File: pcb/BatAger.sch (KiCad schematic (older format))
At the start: 23 parts

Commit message: Added multiple schematic pages.
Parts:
- removed D? (x2): LED, symbol LED
- removed IC?: ATMEGA328-P, DIL28, symbol ATMEGA328-P
- removed OP?: LT1097, symbol LT1097
- removed Q? (x2): BC849, SOT-23, symbol BC849
- removed Q?: CSD18536KCS, TO-220, symbol BTS141
- removed Q?: IRF9530, TO-220, symbol IRF9530
- removed R? (x13): R, symbol R
- removed U?: LM358DUAL, symbol LM358DUAL
- added IC?: ATMEGA2560-A, TQFP100, symbol ATMEGA2560-A
- added U?: LM7805, symbol LM7805
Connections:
- net labels removed: +15V, -15V, GND, VCC
- wire segments 27 -> 0
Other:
- moved on the sheet: U?

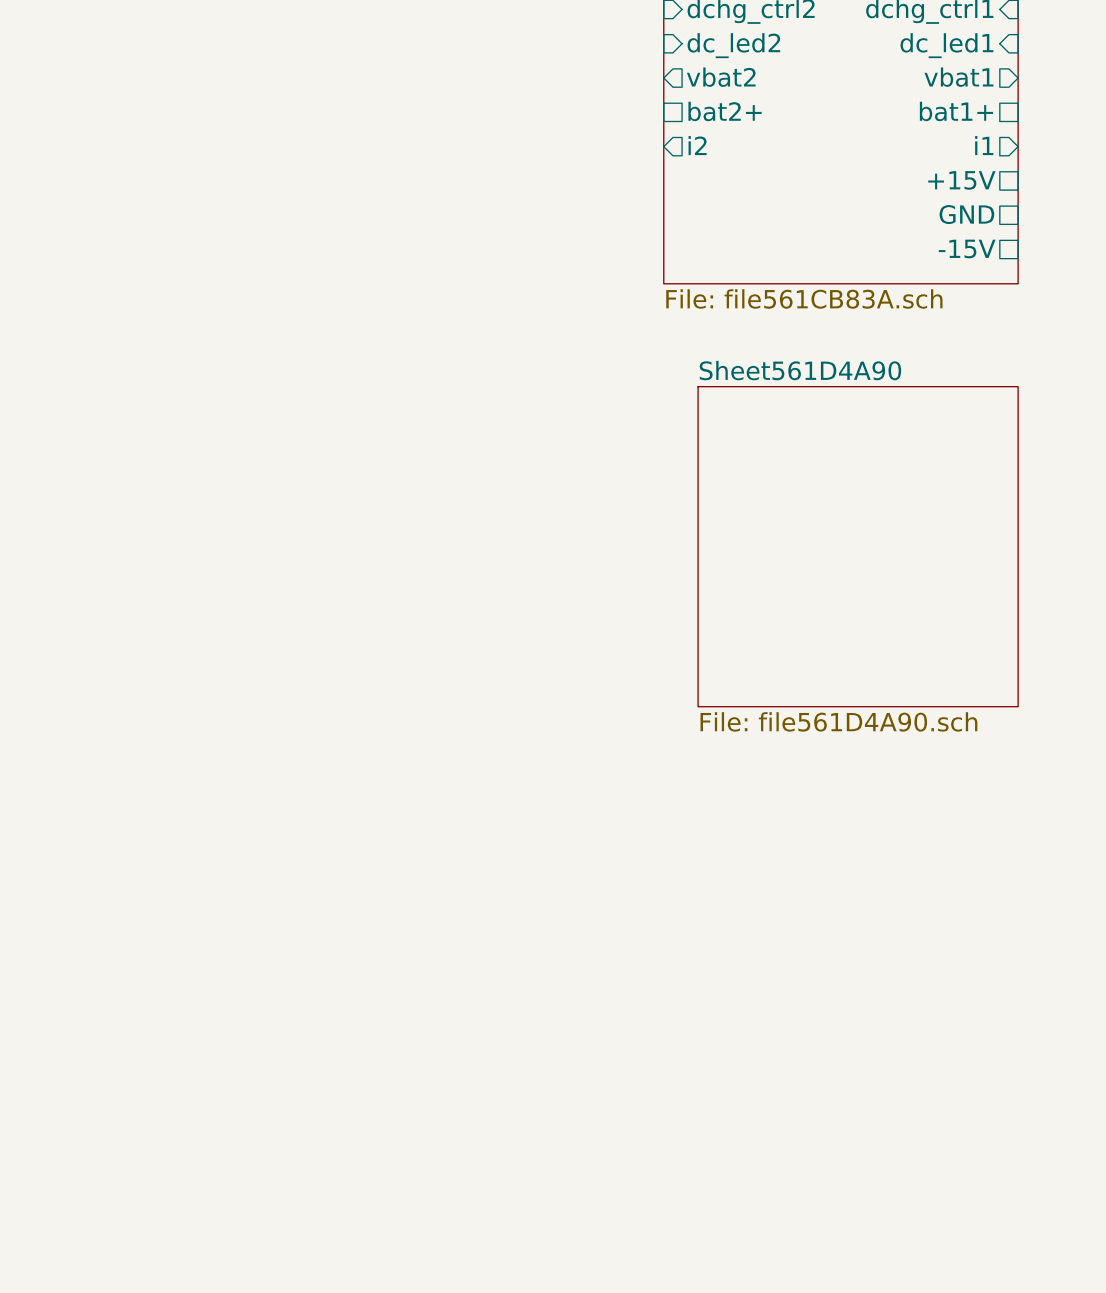
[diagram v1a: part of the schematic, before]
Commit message: updated schematics
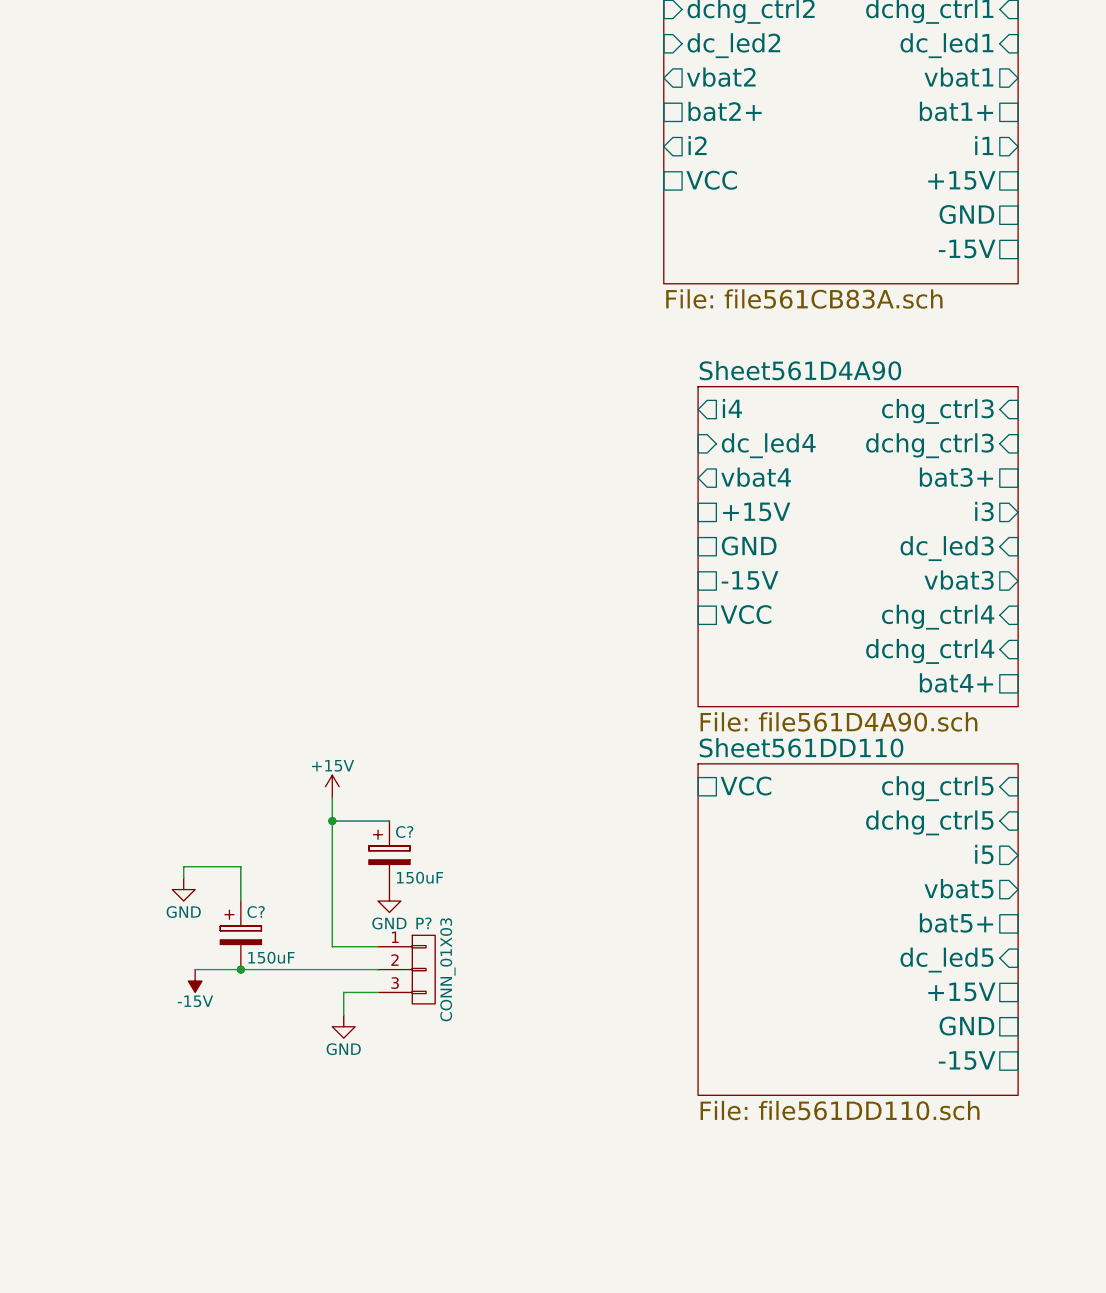
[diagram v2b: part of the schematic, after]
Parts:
- added C? (x2): 150uF, symbol CP
- added P?: CONN_01X03, symbol CONN_01X03
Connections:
- new net +15V: C?.1, P?.1 (P1)
- new net -15V: C?.2, P?.2 (P2)
- new net GND: C?.1, C?.2, P?.3 (P3)
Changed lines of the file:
@@
 $Descr A4 11693 8268
 encoding utf-8
-Sheet 1 3
+Sheet 1 4
 Title ""
 Date "12 oct 2015"
@@
 F15 "bat2+" U L 9050 1750 80
 F16 "i2" O L 9050 1900 80
+F17 "VCC" U L 9050 2050 80
 $EndSheet
 $Sheet
@@
 F0 "Sheet561D4A90" 80
 F1 "file561D4A90.sch" 80
+F2 "chg_ctrl3" I R 10600 3050 80
+F3 "dchg_ctrl3" I R 10600 3200 80
+F4 "bat3+" U R 10600 3350 80
+F5 "i3" O R 10600 3500 80
+F6 "dc_led3" I R 10600 3650 80
+F7 "vbat3" O R 10600 3800 80
+F8 "chg_ctrl4" I R 10600 3950 80
+F9 "dchg_ctrl4" I R 10600 4100 80
+F10 "bat4+" U R 10600 4250 80
+F11 "i4" O L 9200 3050 80
+F12 "dc_led4" I L 9200 3200 80
+F13 "vbat4" O L 9200 3350 80
+F14 "+15V" U L 9200 3500 80
+F15 "GND" U L 9200 3650 80
+F16 "-15V" U L 9200 3800 80
+F17 "VCC" U L 9200 3950 80
 $EndSheet
 $Comp
@@
 	1    0    0    -1
 $EndComp
+$Sheet
+S 9200 4600 1400 1450
+U 561DD111
+F0 "Sheet561DD110" 80
+F1 "file561DD110.sch" 80
+F2 "chg_ctrl5" I R 10600 4700 80
+F3 "dchg_ctrl5" I R 10600 4850 80
+F4 "i5" O R 10600 5000 80
+F5 "vbat5" O R 10600 5150 80
+F6 "bat5+" U R 10600 5300 80
+F7 "dc_led5" I R 10600 5450 80
+F8 "+15V" U R 10600 5600 80
+F9 "GND" U R 10600 5750 80
+F10 "-15V" U R 10600 5900 80
+F11 "VCC" U L 9200 4700 80
+$EndSheet
+$Comp
+L CONN_01X03 P?
+U 1 1 561DFDB9
+P 8000 5500
+F 0 "P?" H 8000 5700 50  0000 C CNN
+F 1 "CONN_01X03" V 8100 5500 50  0000 C CNN
+F 2 "" H 8000 5500 60  0000 C CNN
+F 3 "" H 8000 5500 60  0000 C CNN
+	1    8000 5500
+	1    0    0    -1
+$EndComp
+$Comp
+L +15V #PWR?
+U 1 1 561DFF64
+P 7600 4750
+F 0 "#PWR?" H 7600 4600 50  0001 C CNN
+F 1 "+15V" H 7600 4890 50  0000 C CNN
+F 2 "" H 7600 4750 60  0000 C CNN
+F 3 "" H 7600 4750 60  0000 C CNN
+	1    7600 4750
+	1    0    0    -1
+$EndComp
+$Comp
+L -15V #PWR?
+U 1 1 561E0397
+P 7000 5500
+F 0 "#PWR?" H 7000 5350 50  0001 C CNN
+F 1 "-15V" H 7000 5640 50  0000 C CNN
+F 2 "" H 7000 5500 60  0000 C CNN
+F 3 "" H 7000 5500 60  0000 C CNN
+	1    7000 5500
+	-1   0    0    1
+$EndComp
+$Comp
+L GND #PWR?
+U 1 1 561E075B
+P 7650 5700
+F 0 "#PWR?" H 7650 5450 50  0001 C CNN
+F 1 "GND" H 7650 5550 50  0000 C CNN
+F 2 "" H 7650 5700 60  0000 C CNN
+F 3 "" H 7650 5700 60  0000 C CNN
+	1    7650 5700
+	1    0    0    -1
+$EndComp
+Wire Wire Line
+	7800 5400 7600 5400
+Wire Wire Line
+	7600 5400 7600 4750
+Wire Wire Line
+	7000 5500 7800 5500
+Wire Wire Line
+	7800 5600 7650 5600
+Wire Wire Line
+	7650 5600 7650 5700
+$Comp
+L CP C?
+U 1 1 561E6331
+P 7200 5350
+F 0 "C?" H 7225 5450 50  0000 L CNN
+F 1 "150uF" H 7225 5250 50  0000 L CNN
+F 2 "" H 7238 5200 30  0000 C CNN
+F 3 "" H 7200 5350 60  0000 C CNN
+	1    7200 5350
+	1    0    0    -1
+$EndComp
+Connection ~ 7200 5500
+$Comp
+L GND #PWR?
+U 1 1 561E646E
+P 6950 5100
+F 0 "#PWR?" H 6950 4850 50  0001 C CNN
+F 1 "GND" H 6950 4950 50  0000 C CNN
+F 2 "" H 6950 5100 60  0000 C CNN
+F 3 "" H 6950 5100 60  0000 C CNN
+	1    6950 5100
+	1    0    0    -1
+$EndComp
+Wire Wire Line
+	7200 5200 7200 5050
+Wire Wire Line
+	7200 5050 6950 5050
+Wire Wire Line
+	6950 5050 6950 5100
+$Comp
+L CP C?
+U 1 1 561E67B1
+P 7850 5000
+F 0 "C?" H 7875 5100 50  0000 L CNN
+F 1 "150uF" H 7875 4900 50  0000 L CNN
+F 2 "" H 7888 4850 30  0000 C CNN
+F 3 "" H 7850 5000 60  0000 C CNN
+	1    7850 5000
+	1    0    0    -1
+$EndComp
+$Comp
+L GND #PWR?
+U 1 1 561E68DC
+P 7850 5150
+F 0 "#PWR?" H 7850 4900 50  0001 C CNN
+F 1 "GND" H 7850 5000 50  0000 C CNN
+F 2 "" H 7850 5150 60  0000 C CNN
+F 3 "" H 7850 5150 60  0000 C CNN
+	1    7850 5150
+	1    0    0    -1
+$EndComp
+Wire Wire Line
+	7850 4850 7600 4850
+Connection ~ 7600 4850
 $EndSCHEMATC

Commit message: starting on layout
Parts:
- removed P?: CONN_01X03, symbol CONN_01X03
- removed U? (x2): LM7805, symbol LM7805
- added C1, C2: 47uF, Capacitors_Elko_ThroughHole:Elko_vert_11.2x6.3mm_RM2.5, symbol CP_Small
- added C10, C4, C7, C8, C9: 100nF, Capacitors_SMD:C_0805_HandSoldering, symbol C_Small
- added C3, C5, C6: 22pF, Capacitors_SMD:C_0805_HandSoldering, symbol C_Small
- added CON1: AVR-ISP-6, Pin_Headers:Pin_Header_Straight_2x03, symbol AVR-ISP-6
- added P1: FTDI, Connect:PINHEAD1-6, symbol CONN_01X06
- added P13: -15V, Pin_Headers:Pin_Header_Straight_1x01, symbol CONN_01X01
- added P14: GND, Pin_Headers:Pin_Header_Straight_1x01, symbol CONN_01X01
- added P15: AUX, Pin_Headers:Pin_Header_Straight_1x06, symbol CONN_01X06
- added P2: +15V, Pin_Headers:Pin_Header_Straight_1x01, symbol CONN_01X01
- added P3: BAT1_TP, Pin_Headers:Pin_Header_Straight_1x05, symbol CONN_01X05
- added P4: BAT3_TP, Pin_Headers:Pin_Header_Straight_1x05, symbol CONN_01X05
- added P5: BAT5_TP, Pin_Headers:Pin_Header_Straight_1x05, symbol CONN_01X05
- added P6: BAT2_TP, Pin_Headers:Pin_Header_Straight_1x05, symbol CONN_01X05
- added P7: BAT4_TP, Pin_Headers:Pin_Header_Straight_1x05, symbol CONN_01X05
- added Q1: IRFR3607PBF, TO_SOT_Packages_SMD:TO-252-2Lead, symbol Q_NMOS_GDS
- added R1: 1K, Resistors_SMD:R_0805_HandSoldering, symbol R
- added R2: 10k, Resistors_SMD:R_0805_HandSoldering, symbol R_Small
- added R3: 1M, Resistors_SMD:R_0805_HandSoldering, symbol R
- added R4: 0, Resistors_SMD:R_0805_HandSoldering, symbol R_Small
- added R5, R6: 1K, Resistors_SMD:R_0805_HandSoldering, symbol R_Small
- added SW1: SW_PUSH_4PIN, Buttons_Switches_ThroughHole:SW_PUSH_SMALL, symbol SW_PUSH_4PIN-RESCUE-BatAger
- added U1: MC33269, TO_SOT_Packages_SMD:TO-252-2Lead, symbol MC33269
- added Y1: 16MHz, Crystals:Crystal_HC48-U_Vertical, symbol Crystal
- C11, C12: renamed from C?; footprint (none) -> Capacitors_Elko_ThroughHole:Elko_vert_11.5x8mm_RM3.5
- IC1: renamed from IC?; footprint TQFP100 -> Housings_QFP:TQFP-100_14x14mm_Pitch0.5mm
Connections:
- net labels added: CC1, CC2, CC3, CC4, CC5, DC1, DC2, DC3, DC4, DC5, DCL1, DCL2, DCL3, DCL4, DCL5, GNDPWR, I1, I2, I3, I4, I5, MISO, MOSI, RESET, RST, RX0, RX1, RX2, RX3, SCK, TX0, TX1, TX2, TX3, VBAT1, VBAT2, VBAT3, VBAT4, VBAT5, VCC
- wire segments 9 -> 165
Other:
- note added: "A0"
- note added: "A1"
- note added: "A2"
- note added: "A3"
- note added: "A4"
- note added: "A5"
- note added: "A6"
- note added: "A7"
- note added: "A8"
- note added: "A9"
- note added: "D0"
- note added: "D1"
- note added: "D10"
- note added: "D11"
- note added: "D14"
- note added: "D15"
- note added: "D16"
- note added: "D17"
- note added: "D18"
- note added: "D19"
- note added: "D2"
- note added: "D22"
- note added: "D23"
- note added: "D24"
- note added: "D25"
- note added: "D26"
- note added: "D3"
- note added: "D4"
- note added: "D5"
- note added: "D50"
- note added: "D51"
- note added: "D52"
- note added: "D6"
- note added: "D7"
- note added: "D8"
- note added: "D9"
- moved on the sheet: C12, IC1

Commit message: trace complete (maybe!)
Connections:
- net labels removed: RST
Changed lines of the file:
@@
 	7250 2200 6950 2200
-Wire Wire Line
-	7250 2300 6950 2300
 Wire Wire Line
 	7500 2100 7800 2100
@@
 Text Label 6950 2200 0    40   ~ 0
 SCK
-Text Label 6950 2300 0    40   ~ 0
-RST
 Text Label -1350 4650 0    40   ~ 0
 VCC
@@
 CC2
 Text Label 8800 1150 0    40   ~ 0
-CC1
+CC2
 Text Label 8800 1300 0    40   ~ 0
 DC2
@@
 Text Label 7050 3800 0    40   ~ 0
 RX3
+Wire Wire Line
+	7250 2300 6950 2300
+Text Label 6950 2300 0    40   ~ 0
+RESET
 $EndSCHEMATC

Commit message: adding planes - almost done!
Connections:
- net labels added: fan_ctrl
- wire segments 165 -> 167
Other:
- note added: "D42"
- moved on the sheet: C1, C2, C3, C4, CON1, P1, P15, P3, P4, P5, P6, P7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

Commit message: Production candidate - passes DRC.
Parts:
- C11, C12: footprint Capacitors_Elko_ThroughHole:Elko_vert_11.5x8mm_RM3.5 -> Custom Footprints:Elko_vert_11.5x8mm_RM3.5
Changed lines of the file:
@@
 F 0 "C11" H 7225 5450 50  0000 L CNN
 F 1 "150uF" H 7225 5250 50  0000 L CNN
-F 2 "Capacitors_Elko_ThroughHole:Elko_vert_11.5x8mm_RM3.5" H 7238 5200 30  0001 C CNN
+F 2 "Custom Footprints:Elko_vert_11.5x8mm_RM3.5" H 7238 5200 30  0001 C CNN
 F 3 "" H 7200 5350 60  0000 C CNN
 	1    7200 5350
@@
 F 0 "C12" H 7875 4900 50  0000 L CNN
 F 1 "150uF" H 7875 4700 50  0000 L CNN
-F 2 "Capacitors_Elko_ThroughHole:Elko_vert_11.5x8mm_RM3.5" H 7888 4650 30  0001 C CNN
+F 2 "Custom Footprints:Elko_vert_11.5x8mm_RM3.5" H 7888 4650 30  0001 C CNN
 F 3 "" H 7850 4800 60  0000 C CNN
 	1    7850 4800

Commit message: Changed fan FET (Q22). Many other minor layout changes. Production candidate.
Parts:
- SW1: footprint Buttons_Switches_ThroughHole:SW_PUSH_SMALL -> Custom Footprints:SW_PUSH_4.5x6.5mm
- Y1: footprint Crystals:Crystal_HC48-U_Vertical -> Crystals:Crystal_HC49-U_Vertical
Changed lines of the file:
@@
 F 0 "Y1" H 2750 1800 50  0000 C CNN
 F 1 "16MHz" H 2750 1500 50  0000 C CNN
-F 2 "Crystals:Crystal_HC48-U_Vertical" H 2750 1650 60  0001 C CNN
+F 2 "Crystals:Crystal_HC49-U_Vertical" H 2750 1650 60  0001 C CNN
 F 3 "" H 2750 1650 60  0000 C CNN
 	1    2750 1650
@@
 F 0 "SW1" H 1700 2710 50  0000 C CNN
 F 1 "SW_PUSH_4PIN" H 1550 2520 50  0000 C CNN
-F 2 "Buttons_Switches_ThroughHole:SW_PUSH_SMALL" H 1550 2600 60  0001 C CNN
+F 2 "Custom Footprints:SW_PUSH_4.5x6.5mm" H 1550 2600 60  0001 C CNN
 F 3 "" H 1550 2600 60  0000 C CNN
 	1    1550 2600
